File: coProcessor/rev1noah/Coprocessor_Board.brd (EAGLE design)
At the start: 101.6 x 101.6 mm, 106 parts, among them IC1 STM32F405RGT6, J1 USB_MINI-B_SMT, J2 79107-08, J4 30320-6002HB, J5 5008730806, Q1 L78M05CV

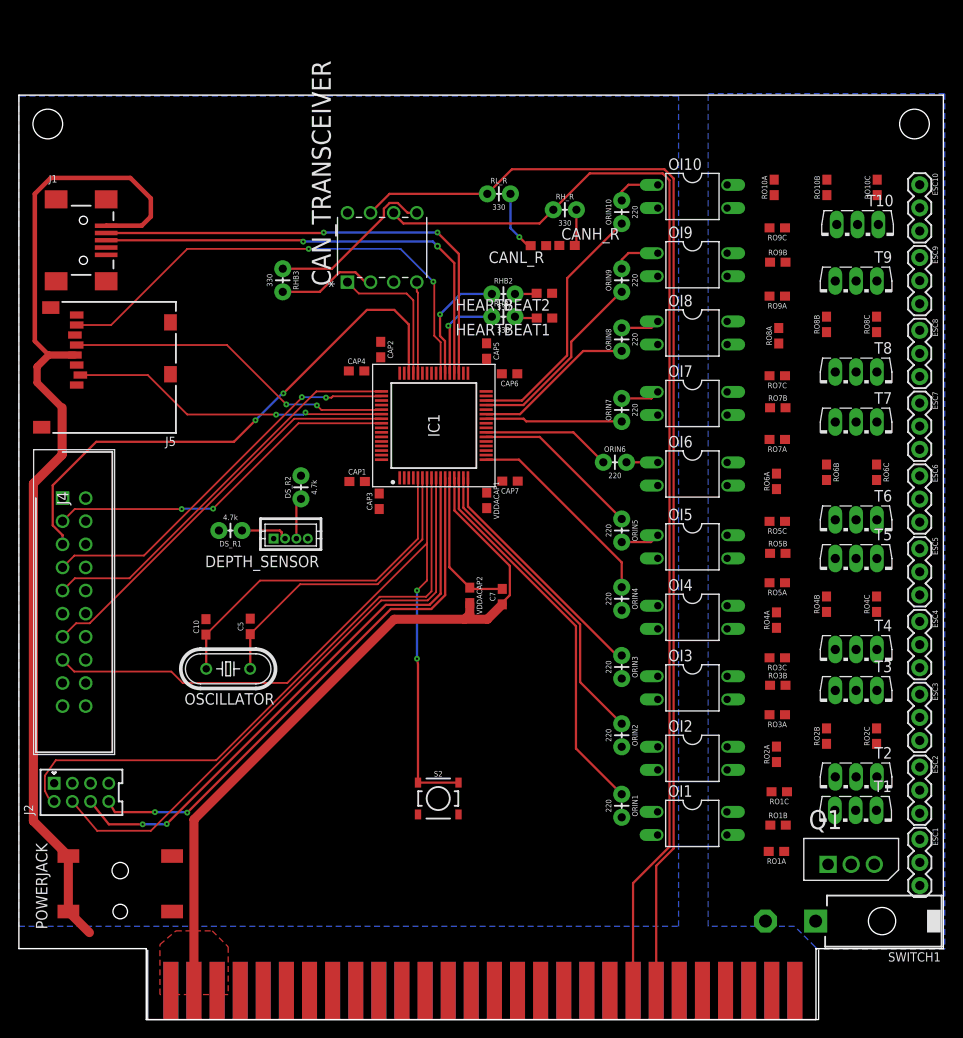
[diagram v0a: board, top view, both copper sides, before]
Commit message: coprocessor board tentatively finished draft2, many things fixed, CAN kicked the can, and parts list added
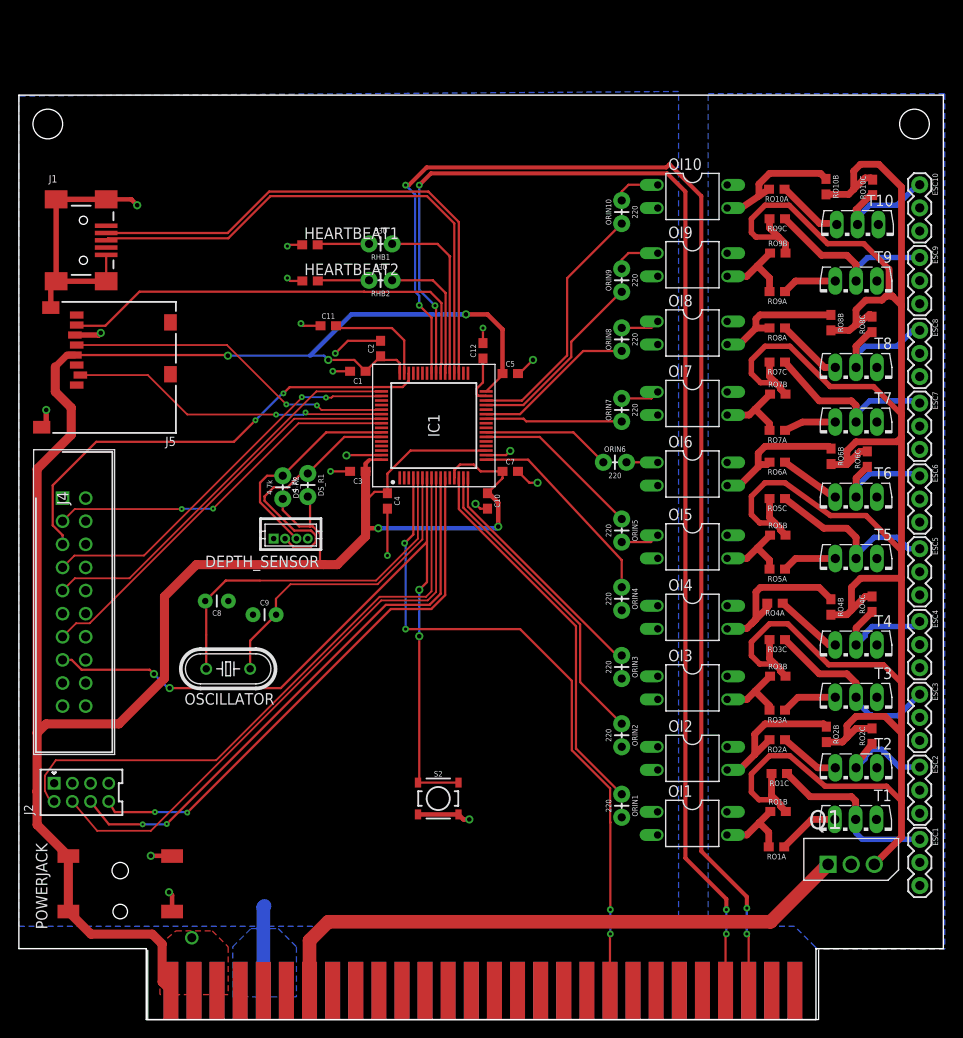
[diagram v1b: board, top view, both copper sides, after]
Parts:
- removed CANH_R, CANL_R: LTST-S270GKT, LTST-S270GKT:0603
- removed CAN_TRANSCEIVER: MCP2551-I/P, MCP2551-I_P:DIP254P762X432-8
- removed CAP1, CAP2, CAP3, CAP4, VDDACAP1: 100nF, SparkFun-Capacitors:0603
- removed CAP5, CAP6: 2.2uF, SparkFun-Capacitors:0603
- removed CAP7: 4.7uF, SparkFun-Capacitors:0603
- removed RHB3, RH_R, RL_R: 330, SparkFun-Resistors:AXIAL-0.1
- removed SWITCH1: 39-30-02?, con-molex-mini-fit:39-30-?02?
- removed VDDACAP2: 1uF, SparkFun-Capacitors:0603
- added C1: 4.7 uF, SparkFun-Capacitors:0603
- added C11: 2.2uF, SparkFun-Capacitors:0603
- added C12: 2.2 uF, SparkFun-Capacitors:0603
- added C2, C3, C4: 100 nF, SparkFun-Capacitors:0603
- added C8, C9: 1 nF, SparkFun-Capacitors:CAP-PTH-2.54
- C10, C5: value 1nF -> 100 nF
- C7: value .1 uF -> 1 uF
- moved C5 39.9 mm to (54.0, 71.0), turned to 0 degrees
- moved C10 33.9 mm to (51.5, 57.0), turned to 270 degrees
- moved HEARTBEAT1 27.0 mm to (32.0, 85.1), turned to 0 degrees
- moved HEARTBEAT2 25.8 mm to (32.0, 81.2), turned to 0 degrees
- moved RHB1 15.7 mm to (39.8, 85.2), turned to 180 degrees
- moved C7 13.8 mm to (54.0, 60.2), turned to 0 degrees
- moved RHB2 13.6 mm to (39.8, 81.2), turned to 180 degrees
- moved DS_R1 9.86 mm to (31.8, 58.8), turned to 270 degrees
- moved RO5C 2.50 mm to (83.3, 57.3)
- moved T6 2.50 mm to (92.0, 56.2)
- moved RO6A 2.11 mm to (83.3, 61.3), turned to 180 degrees
- moved DS_R2 2.00 mm to (29.0, 58.5), turned to 270 degrees
- moved RO1C 2.00 mm to (83.6, 27.0)
- moved RO3C 2.00 mm to (83.3, 41.8)
- moved RO5B 2.00 mm to (83.4, 53.2)
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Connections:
- net T1 renamed GATE1
- net T10 renamed GATE10
- net T2 renamed GATE2
- net T3 renamed GATE3
- net T4 renamed GATE4
- net T5 renamed GATE5
- net T6 renamed GATE6
- net T7 renamed GATE7
- net T8 renamed GATE8
- net T9 renamed GATE9
- removed net 18_22V: Q1.1, SWITCH1.2, U$1.EXTRA23
- removed net CANL: CAN_TRANSCEIVER.7, RL_R.P$1, U$1.CAN_L
- removed net CANRX_BKPLN: CAN_TRANSCEIVER.4, IC1.44
- removed net CANTX-BKPLN: CAN_TRANSCEIVER.1, IC1.45
- removed net N$12: CAN_TRANSCEIVER.5, RHB3.P$1
- removed net N$5: CAN_TRANSCEIVER.2, RHB3.P$2
- removed net N$8: CANL_R.2, RL_R.P$2
- removed net N$9: CANH_R.2, RH_R.P$2
- removed net POWER1O1: RO1B.2, RO1C.2
- removed net POWER1O10: RO10B.2, RO10C.2
- removed net POWER1O2: RO2B.2, RO2C.2
- removed net POWER1O3: RO3B.2, RO3C.2
- removed net POWER1O4: RO4B.2, RO4C.2
- removed net POWER1O5: RO5B.2, RO5C.2
- removed net POWER1O6: RO6B.2, RO6C.2
- removed net POWER1O7: RO7B.2, RO7C.2
- removed net POWER1O8: RO8B.2, RO8C.2
- removed net POWER1O9: RO9B.2, RO9C.2
- removed net VCAP_2_1: CAP5.1, CAP6.1, IC1.31, IC1.47
- new net 18V: Q1.1, U$1.EXTRA23
- new net SOURCE1: ESC1.1, RO1C.1, T1.2
- new net SOURCE10: ESC10.1, RO10C.1, T10.2
- new net SOURCE2: ESC2.1, RO2C.1, T2.2
- new net SOURCE3: ESC3.1, RO3C.1, T3.2
- new net SOURCE4: ESC4.1, RO4C.1, T4.2
- new net SOURCE5: ESC5.1, RO5C.1, T5.2
- new net SOURCE6: ESC6.1, RO6C.1, T6.2
- new net SOURCE7: ESC7.1, RO7C.1, T7.2
- new net SOURCE8: ESC8.1, RO8C.1, T8.2
- new net SOURCE9: ESC9.1, RO9C.1, T9.2
- new net VBUS: J1.VBUS
- new net VCAP: C11.2, IC1.47
- new net VCAP2: C12.1, IC1.31
- net 3.3V: now also C1.1, C10.1, C2.1, C3.1, C4.1, C5.1; no longer CAN_TRANSCEIVER.3, CAP1.1, CAP2.1, CAP3.1, CAP4.1, CAP7.1, J1.VBUS, VDDACAP1.2, VDDACAP2.2
- net 5V: now also RO10B.2, RO10C.2, RO1B.2, RO1C.2, RO2B.2, RO2C.2, RO3B.2, RO3C.2, RO4B.2, RO4C.2, RO5B.2, RO5C.2, RO6B.2, RO6C.2, RO7B.2, RO7C.2, RO8B.2, RO8C.2, RO9B.2, RO9C.2; no longer ESC1.1, ESC10.1, ESC2.1, ESC3.1, ESC4.1, ESC5.1, ESC6.1, ESC7.1, ESC8.1, ESC9.1, RO10C.1, RO1C.1, RO2C.1, RO3C.1, RO4C.1, RO5C.1, RO6C.1, RO7C.1, RO8C.1, RO9C.1, T1.2, T10.2, T2.2, T3.2, T4.2, T5.2, T6.2, T7.2, T8.2, T9.2
- net CANH: no longer CAN_TRANSCEIVER.6, RH_R.P$1
- net GND: now also C1.2, C11.1, C12.2, C2.2, C3.2, C4.2, C8.1, C9.1; no longer CANH_R.1, CANL_R.1, CAP1.2, CAP2.2, CAP3.2, CAP4.2, CAP5.2, CAP6.2, CAP7.2, VDDACAP1.1, VDDACAP2.1
- net GNDBAT: no longer SWITCH1.1
- net RCC_OSC_IN: now also C8.2; no longer C10.1
- net RCC_OSC_OUT: now also C9.2; no longer C5.1
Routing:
- net 5V: track 0.00 -> 291.7 mm
- net SCL_BKPLN: track 0.00 -> 146.2 mm, vias 0 -> 4
- net SDA_BKPLN: track 0.00 -> 141.8 mm, vias 0 -> 4
- net CANL: track 125.8 -> 0.00 mm
- net CANH: track 124.2 -> 0.00 mm
- net 3.3V: track 193.2 -> 273.1 mm, vias 0 -> 6
- net KILLSWITCH: track 0.00 -> 73.5 mm, vias 0 -> 4
- net GND: track 19.0 -> 92.3 mm, vias 0 -> 19
- net 18V: track 0.00 -> 66.0 mm
- net DEPTHSDA: track 5.29 -> 27.9 mm
- net SOURCE9: track 0.00 -> 20.6 mm
- net SOURCE3: track 0.00 -> 20.4 mm
- net SOURCE5: track 0.00 -> 20.3 mm
- net SOURCE7: track 0.00 -> 20.3 mm
- net SOURCE1: track 0.00 -> 19.6 mm
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
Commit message: General clean (salute) up of copro
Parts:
- removed HEARTBEAT1, HEARTBEAT2: LTST-S270GKT, LTST-S270GKT:0603
- removed J2: 79107-08, con-molex-milli-grid:79107-08
- removed S2: MOMENTARY-SWITCH-SPST-SMD-4.5MM, SparkFun-Switches:TACTILE_SWITCH_SMD_4.5MM
- added HBL1, HBL2: LED, SparkFun-Resistors:AXIAL-0.1
- added P1: 39-30-08?, con-molex-mini-fit:39-30-?08?
- added RESET: (no value), switch-omron:B3F-10XX
- moved J4 24.3 mm to (29.0, 59.6), turned to 180 degrees
- moved DEPTH_SENSOR 12.2 mm to (21.3, 44.2)
- moved OSCILLATOR 12.1 mm to (34.9, 41.1)
- moved C9 11.6 mm to (38.5, 45.5), turned to 180 degrees
- moved DS_R2 9.56 mm to (26.0, 49.4)
- moved DS_R1 9.49 mm to (29.5, 49.5)
- moved C8 9.41 mm to (31.1, 45.5), turned to 0 degrees
- moved C11 8.43 mm to (42.4, 75.3), turned to 270 degrees
- moved RO2C 8.01 mm to (86.5, 27.7), turned to 180 degrees
- moved RO8C 7.30 mm to (86.5, 77.0), turned to 180 degrees
- moved RO4C 7.28 mm to (86.5, 45.2), turned to 180 degrees
- moved RO1C 7.23 mm to (86.7, 20.5)
- moved RO8B 6.98 mm to (82.3, 77.4), turned to 90 degrees
- moved RO6B 6.95 mm to (82.3, 62.3), turned to 90 degrees
- moved RO10C 6.82 mm to (87.1, 92.2), turned to 180 degrees
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- renumbered POWERJACK to 3V3_ONLY
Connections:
- removed net N$10: HEARTBEAT1.2, RHB1.P$2
- removed net POWER: U$1.3.3V_4, U$1.3.3V_5, U$1.3.3V_6
- new net N$1: HBL1.P$1, RHB1.P$2
- net 3.3V: now also P1.1, P1.2, P1.3, P1.4, U$1.3.3V_4, U$1.3.3V_5, U$1.3.3V_6; no longer J2.1, J2.3, J2.5, J2.7
- net DEPTHSCL: now also DEPTH_SENSOR.P$2; no longer DEPTH_SENSOR.P$3
- net DEPTHSDA: now also DEPTH_SENSOR.P$3; no longer DEPTH_SENSOR.P$2
- net GND: now also HBL1.P$2, HBL2.P$2, RESET.2; no longer HEARTBEAT1.1, HEARTBEAT2.1, S2.2, S2.3
- net JTAG15: now also RESET.3, RESET.4; no longer S2.1, S2.4
- net MISSION_START: now also P1.8; no longer J2.2
- net N$14: now also HBL2.P$1; no longer HEARTBEAT2.2
- net SDIO_CMD: now also J5.3; no longer J5.2
- net SWITCH_3: now also P1.7; no longer J2.4
- net SWITCH_4: now also P1.6; no longer J2.6
- net SWITCH_5: now also P1.5; no longer J2.8
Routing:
- net GNDBAT: track 0.00 -> 63.7 mm, vias 0 -> 1
- net 5V: track 291.7 -> 241.8 mm
- net JTAG15: track 87.0 -> 56.4 mm, vias 4 -> 2
- net SYS_JTMS-SWIDIO: track 51.7 -> 25.3 mm, vias 2 -> 1
- net 3.3V: track 273.1 -> 298.0 mm, vias 6 -> 5
- net SYS_JTRST: track 39.5 -> 15.9 mm, vias 2 -> 0
- net MISSION_START: track 66.9 -> 45.0 mm
- net GND: track 92.3 -> 112.3 mm, vias 19 -> 16
- net SYS_JTDI: track 42.9 -> 23.7 mm, vias 2 -> 0
- net SYS_JTCK-SWCLK: track 44.1 -> 26.4 mm
- net SWITCH_3: track 64.9 -> 48.6 mm
- net RCC_OSC_IN: track 40.4 -> 25.6 mm
- net SYS_JTDO-SWO: track 45.0 -> 30.6 mm
- net RCC_OSC_OUT: track 34.5 -> 22.3 mm
- net POWER2O4: track 18.6 -> 8.48 mm
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- added copper zone on layer 16, net 3.3V
- added copper zone on layer 1, net GND
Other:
- board text added: "HPA"
- board text added: "HPF"
- board text added: "HSA"
- board text added: "HSF"
- board text added: "SPH"
- board text added: "SPL"
- board text added: "SSH"
- board text added: "SSL"
- board text added: "START"
- board text added: "SW3 SW4 SW5"
- board text added: "SWA"
- board text added: "SWF"
